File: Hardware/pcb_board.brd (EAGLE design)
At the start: 170.2 x 111.2 mm, 103 parts, among them IC1 XC6220A331MR-G, IC3 BD5229G-TR, J1 SAMACSYS_PARTS_USB4110-GF-A, J2 112A-TAAR-R03_ATTEND, J3 FH34SRJ-24S-0.5SH_99_, J4 QWIIC_RIGHT_ANGLE, Q1 20V/4.2A/52mΩ/1.4W, Q2 SI1308EDL-T1-GE3, Q3 20V/4.2A/52mΩ/1.4W, U1 MCP73831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

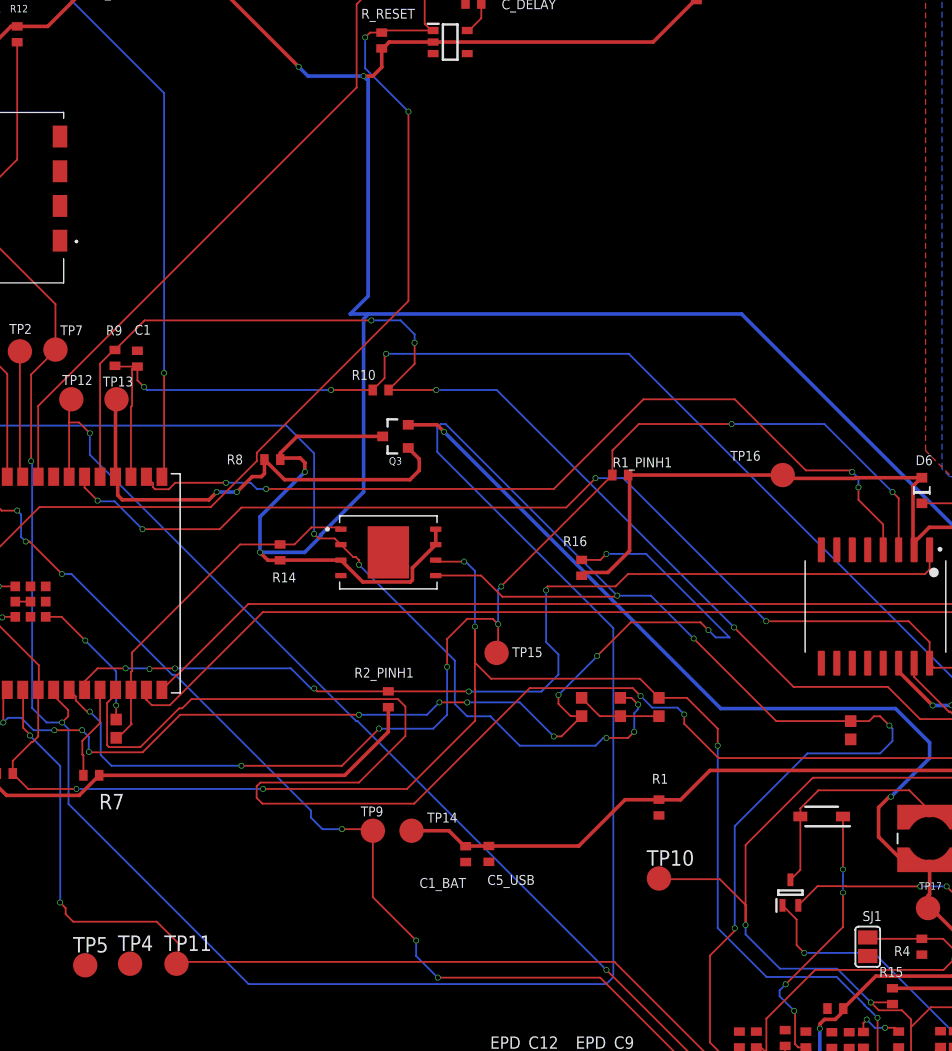
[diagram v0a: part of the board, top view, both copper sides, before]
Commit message: Resolve Issue 1 2 and add battery cable
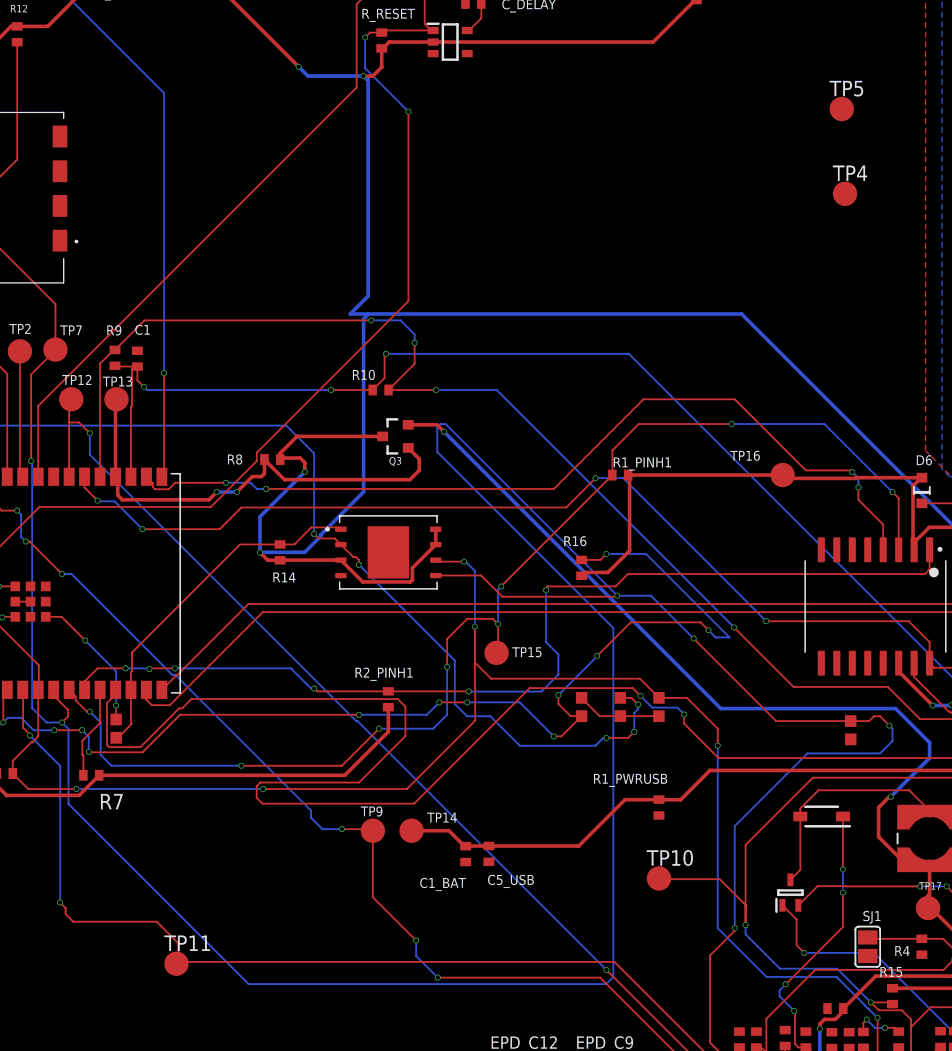
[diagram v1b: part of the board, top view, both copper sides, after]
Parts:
- D2: value ESP32_WROVER_AVX---SD0805S020S1R0_AVX_SD0805S020S1R0_0_0AVX_SD0805S020S1R0_0_0 -> SD0805S020S1R0
- U3: value BME680 -> BME688
- moved TP5 93.8 mm to (80.4, 96.1)
- moved TP4 86.3 mm to (80.7, 89.1)
- renumbered R1 to R1_PWRUSB
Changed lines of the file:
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@@
 <attribute name="VALUE" x="54.575" y="45.215" size="0.6096" layer="27" align="top-left"/>
 </element>
-<element name="D2" library="DeskAssistant_v19_v1" library_urn="urn:adsk.wipprod:fs.file:vf.q_BEPzLFRl2sBZ4D8EmW4Q" package="ESP32_WROVER_AVX---SD0805S020S1R0_AVX_SD0805S020S1R0_0" value="ESP32_WROVER_AVX---SD0805S020S1R0_AVX_SD0805S020S1R0_0_0AVX_SD0805S020S1R0_0_0" x="135.89" y="46.355" smashed="yes" rot="R180">
+<element name="D2" library="DeskAssistant_v19_v1" library_urn="urn:adsk.wipprod:fs.file:vf.q_BEPzLFRl2sBZ4D8EmW4Q" package="ESP32_WROVER_AVX---SD0805S020S1R0_AVX_SD0805S020S1R0_0" value="SD0805S020S1R0" x="135.89" y="46.355" smashed="yes" rot="R180">
 <attribute name="CENTROID_NOT_SPECIFIED" value="No" x="101.6" y="150.495" size="1.778" layer="27" rot="R180" display="off"/>
 <attribute name="DATASHEET" value="http://datasheets.avx.com/schottky.pdf" x="101.6" y="150.495" size="1.778" layer="27" rot="R180" display="off"/>
@@
 <attribute name="PROD_ID" value="TRAN-14388" x="79.375" y="150.495" size="1.778" layer="27" rot="R90" display="off"/>
 </element>
-<element name="R1" library="DeskAssistant_v19_v1" library_urn="urn:adsk.wipprod:fs.file:vf.q_BEPzLFRl2sBZ4D8EmW4Q" package="ESP32_WROVER_EAGLE-LTSPICE_R0402" value="100k" x="65.405" y="38.735" smashed="yes" rot="R90">
+<element name="R1_PWRUSB" library="DeskAssistant_v19_v1" library_urn="urn:adsk.wipprod:fs.file:vf.q_BEPzLFRl2sBZ4D8EmW4Q" package="ESP32_WROVER_EAGLE-LTSPICE_R0402" value="100k" x="65.405" y="38.735" smashed="yes" rot="R90">
 <attribute name="NAME" x="66.16" y="41.5" size="0.8128" layer="25" rot="R180"/>
 <attribute name="SPICEMODEL" value="NONE" x="150.495" y="62.865" size="1.778" layer="27" rot="R90" display="off"/>
@@
 <attribute name="VALUE" x="140.462" y="20.574" size="0.0254" layer="27"/>
 </element>
-<element name="TP4" library="DeskAssistant_v19_v1" library_urn="urn:adsk.wipprod:fs.file:vf.q_BEPzLFRl2sBZ4D8EmW4Q" package="TP20R" value="TPTP20R" x="21.971" y="25.908" smashed="yes">
-<attribute name="NAME" x="20.971" y="26.958" size="1.27" layer="25"/>
-<attribute name="POPULARITY" value="2" x="108.331" y="-64.262" size="1.778" layer="27" display="off"/>
-<attribute name="TP_SIGNAL_NAME" value="" x="21.971" y="23.368" size="1" layer="37"/>
-<attribute name="VALUE" x="21.209" y="24.892" size="0.0254" layer="27"/>
-</element>
-<element name="TP5" library="DeskAssistant_v19_v1" library_urn="urn:adsk.wipprod:fs.file:vf.q_BEPzLFRl2sBZ4D8EmW4Q" package="TP20R" value="TPTP20R" x="18.288" y="25.781" smashed="yes">
-<attribute name="NAME" x="17.288" y="26.831" size="1.27" layer="25"/>
-<attribute name="POPULARITY" value="2" x="109.728" y="-64.389" size="1.778" layer="27" display="off"/>
-<attribute name="TP_SIGNAL_NAME" value="" x="18.288" y="23.241" size="1" layer="37"/>
-<attribute name="VALUE" x="17.526" y="24.765" size="0.0254" layer="27"/>
+<element name="TP4" library="DeskAssistant_v19_v1" library_urn="urn:adsk.wipprod:fs.file:vf.q_BEPzLFRl2sBZ4D8EmW4Q" package="TP20R" value="TPTP20R" x="80.691" y="89.138" smashed="yes">
+<attribute name="NAME" x="79.691" y="90.188" size="1.27" layer="25"/>
+<attribute name="POPULARITY" value="2" x="167.051" y="-1.032" size="1.778" layer="27" display="off"/>
+<attribute name="TP_SIGNAL_NAME" value="" x="80.691" y="86.598" size="1" layer="37"/>
+<attribute name="VALUE" x="79.929" y="88.122" size="0.0254" layer="27"/>
+</element>
+<element name="TP5" library="DeskAssistant_v19_v1" library_urn="urn:adsk.wipprod:fs.file:vf.q_BEPzLFRl2sBZ4D8EmW4Q" package="TP20R" value="TPTP20R" x="80.418" y="96.101" smashed="yes">
+<attribute name="NAME" x="79.418" y="97.151" size="1.27" layer="25"/>
+<attribute name="POPULARITY" value="2" x="171.858" y="5.931" size="1.778" layer="27" display="off"/>
+<attribute name="TP_SIGNAL_NAME" value="" x="80.418" y="93.561" size="1" layer="37"/>
+<attribute name="VALUE" x="79.656" y="95.085" size="0.0254" layer="27"/>
 </element>
 <element name="TP6" library="DeskAssistant_v19_v1" library_urn="urn:adsk.wipprod:fs.file:vf.q_BEPzLFRl2sBZ4D8EmW4Q" package="TP20R" value="TPTP20R" x="6.35" y="102.87" smashed="yes">
@@
 <attribute name="VALUE" x="2.569" y="46.566" size="0.8128" layer="27" rot="R270"/>
 </element>
-<element name="U3" library="DeskAssistant_v19_v1" library_urn="urn:adsk.wipprod:fs.file:vf.q_BEPzLFRl2sBZ4D8EmW4Q" package="ESP32_WROVER_BME680_PSON80P300X300X100-8N" value="BME680" x="154.305" y="19.05" smashed="yes" rot="R180">
+<element name="U3" library="DeskAssistant_v19_v1" library_urn="urn:adsk.wipprod:fs.file:vf.q_BEPzLFRl2sBZ4D8EmW4Q" package="ESP32_WROVER_BME680_PSON80P300X300X100-8N" value="BME688" x="154.305" y="19.05" smashed="yes" rot="R180">
 <attribute name="AVAILABILITY" value="Unavailable" x="81.915" y="68.58" size="1.778" layer="27" rot="R180" display="off"/>
 <attribute name="DESCRIPTION" value=" Integrated Environmental Unit " x="81.915" y="68.58" size="1.778" layer="27" rot="R180" display="off"/>
@@
 <contactref element="C1_BAT1" pad="2"/>
 <contactref element="IC1" pad="2"/>
-<contactref element="R1" pad="1"/>
+<contactref element="R1_PWRUSB" pad="1"/>
 <contactref element="J2" pad="G1"/>
 <contactref element="J2" pad="G2"/>
@@
 <contactref element="Q1" pad="1"/>
 <contactref element="D2" pad="2"/>
-<contactref element="R1" pad="2"/>
+<contactref element="R1_PWRUSB" pad="2"/>
 <contactref element="U1" pad="4"/>
 <contactref element="LED1" pad="A"/>
